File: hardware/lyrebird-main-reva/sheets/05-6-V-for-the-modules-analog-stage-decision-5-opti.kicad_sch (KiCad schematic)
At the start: 6 parts, among them U7 LMR33630 12V->-6V inverting

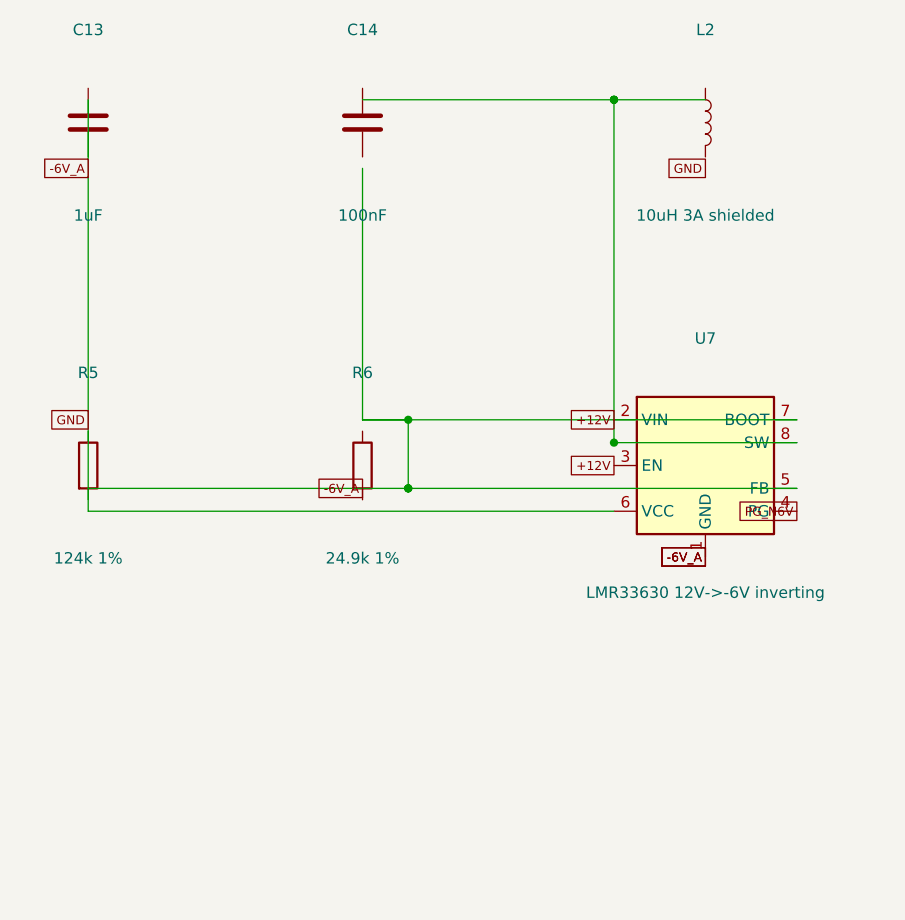
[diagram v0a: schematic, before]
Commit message: Connect two power-good nets that were connected to nothing
The schematic validator found a confirmed fault, and it is the kind that
reads as correct code. `Net("PG_5V")` appears twice in main_board.py --
once to attach the buck's power-good pin, once to attach its pull-up --
and SKiDL creates a NEW net on each call, uniquifying the second name.
The result was four single-node nets: both LMR33630 power-good pins
alone, and both 100 k resistors with one lead floating.

The inverter's half mattered more than the buck's. U7's GND pin *is*
-6V_A, so 100 k to system ground is a pull-up relative to the device and
the only way that flag can be read at all. It was reading nothing.

Both now use one Net object and reuse it, which is what every other net
in both generators already did -- the defect was exactly two instances of
one idiom, not a pattern. I checked: MCLK is also written as
Net("MCLK") twice, but once per file on different boards, so it is
whole in each netlist.

The more useful outcome is a check. A net with one node connects
nothing, and nothing in the generation path said so -- KiCad ERC would
have, on import, and nothing runs ERC. check_freshness.py now reports
single-node nets on both boards, with the module's four reserved element
lines exempted because interface.md requires the main board to drive
them and they are correctly bare on the module side. Tamper-tested by
reintroducing the idiom: it names PG_5V and PG_5V1 and fails.

Co-Authored-By: Claude Opus 5 <noreply@anthropic.com>
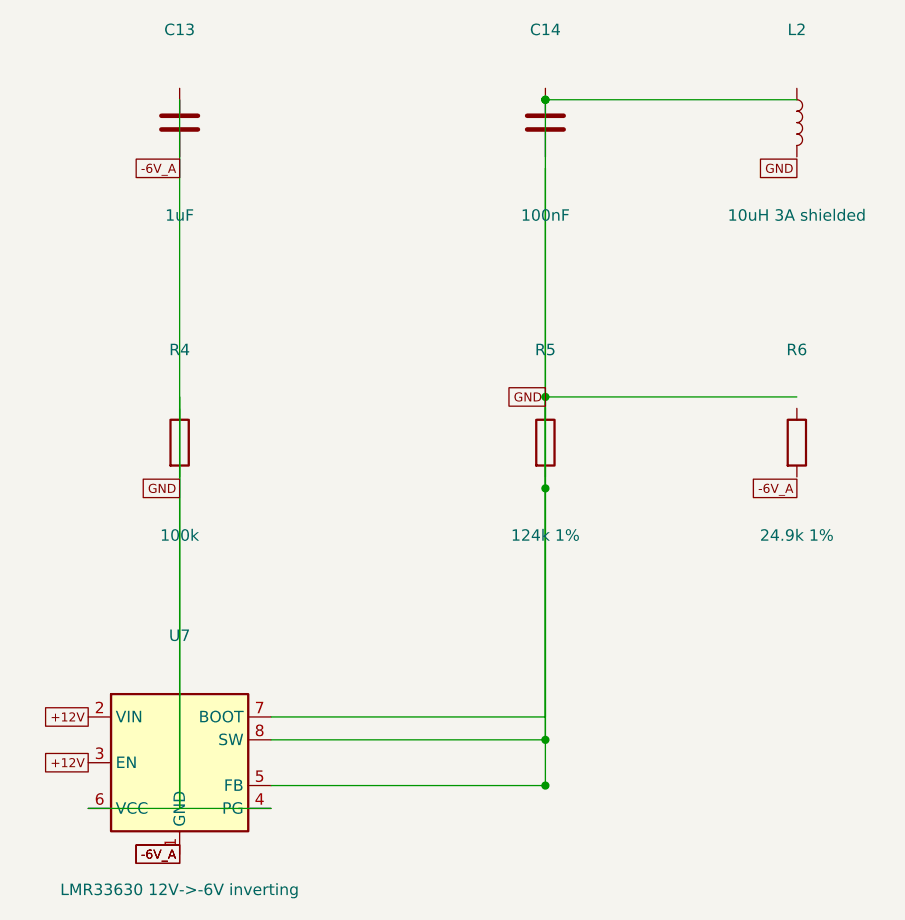
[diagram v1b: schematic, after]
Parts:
- added U7: LMR33630 12V->-6V inverting, symbol Regulator_Switching:LMR33630ADDA
- R4: renamed from R5; value 124k 1% -> 100k
- R5: renamed from R6; value 24.9k 1% -> 124k 1%
- R6: renamed from U7; value LMR33630 12V->-6V inverting -> 24.9k 1%; symbol Regulator_Switching:LMR33630ADDA -> Device:R
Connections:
- net +12V: now also U7.2 (VIN), U7.3 (EN); no longer R6.1 (GND), R6.2 (VIN), R6.3 (EN), R6.5 (FB), R6.6 (VCC), R6.7 (BOOT), R6.8 (SW), R6.9 (GND)
- removed net PG_N6V: R6.4 (PG)
- new net -6V_A: U7.1 (GND), U7.4 (PG), U7.5 (FB), U7.6 (VCC), U7.7 (BOOT), U7.8 (SW), U7.9 (GND)
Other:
- moved on the sheet: C13, C14, L2, R4, R5
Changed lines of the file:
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@@
 	(version 20231120)
 	(generator "lyrebird")
-	(paper "User" 164 115)
+	(paper "User" 164 148)
 	(title_block (title "6 V for the module's analog stage (decision 5, option B)"))
-	(symbol (lib_id "Device:C") (at 35.56 35.56 0) (unit 1)
+	(symbol (lib_id "Device:C") (at 45.72 35.56 0) (unit 1)
 		(exclude_from_sim no) (in_bom yes) (on_board yes) (dnp no)
-		(property "Reference" "C13" (at 35.56 25.250000000000004 0)
+		(property "Reference" "C13" (at 45.72 25.250000000000004 0)
 			(effects (font (size 1.27 1.27))))
-		(property "Value" "1uF" (at 35.56 45.870000000000005 0)
+		(property "Value" "1uF" (at 45.72 45.870000000000005 0)
 			(effects (font (size 1.27 1.27))))
 		(instances (project "" (path "/" (reference "C13") (unit 1))))
 	)
-	(symbol (lib_id "Device:C") (at 66.04 35.56 0) (unit 1)
+	(symbol (lib_id "Device:C") (at 86.36 35.56 0) (unit 1)
 		(exclude_from_sim no) (in_bom yes) (on_board yes) (dnp no)
-		(property "Reference" "C14" (at 66.04 25.250000000000004 0)
+		(property "Reference" "C14" (at 86.36 25.250000000000004 0)
 			(effects (font (size 1.27 1.27))))
-		(property "Value" "100nF" (at 66.04 45.870000000000005 0)
+		(property "Value" "100nF" (at 86.36 45.870000000000005 0)
 			(effects (font (size 1.27 1.27))))
 		(instances (project "" (path "/" (reference "C14") (unit 1))))
 	)
-	(symbol (lib_id "Device:L") (at 104.14 35.56 0) (unit 1)
+	(symbol (lib_id "Device:L") (at 114.3 35.56 0) (unit 1)
 		(exclude_from_sim no) (in_bom yes) (on_board yes) (dnp no)
-		(property "Reference" "L2" (at 104.14 25.250000000000004 0)
+		(property "Reference" "L2" (at 114.3 25.250000000000004 0)
 			(effects (font (size 1.27 1.27))))
-		(property "Value" "10uH 3A shielded" (at 104.14 45.870000000000005 0)
+		(property "Value" "10uH 3A shielded" (at 114.3 45.870000000000005 0)
 			(effects (font (size 1.27 1.27))))
 		(instances (project "" (path "/" (reference "L2") (unit 1))))
 	)
-	(symbol (lib_id "Device:R") (at 35.56 73.66 0) (unit 1)
+	(symbol (lib_id "Device:R") (at 45.72 71.12 0) (unit 1)
 		(exclude_from_sim no) (in_bom yes) (on_board yes) (dnp no)
-		(property "Reference" "R5" (at 35.56 63.349999999999994 0)
+		(property "Reference" "R4" (at 45.72 60.81 0)
 			(effects (font (size 1.27 1.27))))
-		(property "Value" "124k 1%" (at 35.56 83.97 0)
+		(property "Value" "100k" (at 45.72 81.43 0)
+			(effects (font (size 1.27 1.27))))
+		(instances (project "" (path "/" (reference "R4") (unit 1))))
+	)
+	(symbol (lib_id "Device:R") (at 86.36 71.12 0) (unit 1)
+		(exclude_from_sim no) (in_bom yes) (on_board yes) (dnp no)
+		(property "Reference" "R5" (at 86.36 60.81 0)
+			(effects (font (size 1.27 1.27))))
+		(property "Value" "124k 1%" (at 86.36 81.43 0)
 			(effects (font (size 1.27 1.27))))
 		(instances (project "" (path "/" (reference "R5") (unit 1))))
 	)
-	(symbol (lib_id "Device:R") (at 66.04 73.66 0) (unit 1)
+	(symbol (lib_id "Device:R") (at 114.3 71.12 0) (unit 1)
 		(exclude_from_sim no) (in_bom yes) (on_board yes) (dnp no)
-		(property "Reference" "R6" (at 66.04 63.349999999999994 0)
+		(property "Reference" "R6" (at 114.3 60.81 0)
 			(effects (font (size 1.27 1.27))))
-		(property "Value" "24.9k 1%" (at 66.04 83.97 0)
+		(property "Value" "24.9k 1%" (at 114.3 81.43 0)
 			(effects (font (size 1.27 1.27))))
 		(instances (project "" (path "/" (reference "R6") (unit 1))))
 	)
-	(symbol (lib_id "Regulator_Switching:LMR33630ADDA") (at 104.14 73.66 0) (unit 1)
+	(symbol (lib_id "Regulator_Switching:LMR33630ADDA") (at 45.72 106.68 0) (unit 1)
 		(exclude_from_sim no) (in_bom yes) (on_board yes) (dnp no)
-		(property "Reference" "U7" (at 104.14 59.53999999999999 0)
+		(property "Reference" "U7" (at 45.72 92.56 0)
 			(effects (font (size 1.27 1.27))))
-		(property "Value" "LMR33630 12V->-6V inverting" (at 104.14 87.78 0)
+		(property "Value" "LMR33630 12V->-6V inverting" (at 45.72 120.80000000000001 0)
 			(effects (font (size 1.27 1.27))))
 		(instances (project "" (path "/" (reference "U7") (unit 1))))
 	)
-	(wire (pts (xy 71.12 68.58) (xy 71.12 76.2))
+	(wire (pts (xy 86.36 66.04) (xy 86.36 109.22))
 		(stroke (width 0) (type default)))
-	(wire (pts (xy 35.56 76.2) (xy 71.12 76.2))
+	(junction (at 86.36 76.2) (diameter 0)
+		(color 0 0 0 0))
+	(wire (pts (xy 114.3 66.04) (xy 86.36 66.04))
 		(stroke (width 0) (type default)))
-	(junction (at 71.12 76.2) (diameter 0)
+	(junction (at 86.36 66.04) (diameter 0)
 		(color 0 0 0 0))
-	(wire (pts (xy 66.04 68.58) (xy 71.12 68.58))
+	(wire (pts (xy 55.88 109.22) (xy 86.36 109.22))
 		(stroke (width 0) (type default)))
-	(junction (at 71.12 68.58) (diameter 0)
+	(junction (at 86.36 109.22) (diameter 0)
 		(color 0 0 0 0))
-	(wire (pts (xy 114.3 76.2) (xy 71.12 76.2))
+	(wire (pts (xy 45.72 33.02) (xy 45.72 111.76))
 		(stroke (width 0) (type default)))
-	(junction (at 71.12 76.2) (diameter 0)
+	(wire (pts (xy 45.72 111.76) (xy 35.56 111.76))
+		(stroke (width 0) (type default)))
+	(wire (pts (xy 86.36 40.64) (xy 86.36 101.6))
+		(stroke (width 0) (type default)))
+	(wire (pts (xy 86.36 101.6) (xy 55.88 101.6))
+		(stroke (width 0) (type default)))
+	(wire (pts (xy 45.72 66.04) (xy 45.72 111.76))
+		(stroke (width 0) (type default)))
+	(wire (pts (xy 45.72 111.76) (xy 55.88 111.76))
+		(stroke (width 0) (type default)))
+	(wire (pts (xy 86.36 33.02) (xy 86.36 104.14))
+		(stroke (width 0) (type default)))
+	(junction (at 86.36 33.02) (diameter 0)
 		(color 0 0 0 0))
-	(wire (pts (xy 35.56 33.02) (xy 35.56 78.74))
+	(wire (pts (xy 114.3 33.02) (xy 86.36 33.02))
 		(stroke (width 0) (type default)))
-	(wire (pts (xy 35.56 78.74) (xy 93.98 78.74))
+	(junction (at 86.36 33.02) (diameter 0)
+		(color 0 0 0 0))
+	(wire (pts (xy 55.88 104.14) (xy 86.36 104.14))
 		(stroke (width 0) (type default)))
-	(wire (pts (xy 66.04 40.64) (xy 66.04 68.58))
-		(stroke (width 0) (type default)))
-	(wire (pts (xy 66.04 68.58) (xy 114.3 68.58))
-		(stroke (width 0) (type default)))
-	(wire (pts (xy 93.98 33.02) (xy 93.98 71.12))
-		(stroke (width 0) (type default)))
-	(wire (pts (xy 66.04 33.02) (xy 93.98 33.02))
-		(stroke (width 0) (type default)))
-	(junction (at 93.98 33.02) (diameter 0)
+	(junction (at 86.36 104.14) (diameter 0)
 		(color 0 0 0 0))
-	(wire (pts (xy 104.14 33.02) (xy 93.98 33.02))
-		(stroke (width 0) (type default)))
-	(junction (at 93.98 33.02) (diameter 0)
-		(color 0 0 0 0))
-	(wire (pts (xy 114.3 71.12) (xy 93.98 71.12))
-		(stroke (width 0) (type default)))
-	(junction (at 93.98 71.12) (diameter 0)
-		(color 0 0 0 0))
-	(global_label "+12V" (shape passive) (at 93.98 68.58 0)
+	(global_label "+12V" (shape passive) (at 35.56 101.6 0)
 		(effects (font (size 1.0 1.0)) (justify right))
 )
-	(global_label "+12V" (shape passive) (at 93.98 73.66 0)
+	(global_label "+12V" (shape passive) (at 35.56 106.68 0)
 		(effects (font (size 1.0 1.0)) (justify right))
 )
-	(global_label "-6V_A" (shape passive) (at 35.56 40.64 0)
+	(global_label "-6V_A" (shape passive) (at 45.72 40.64 0)
 		(effects (font (size 1.0 1.0)) (justify right))
 )
-	(global_label "-6V_A" (shape passive) (at 66.04 76.2 0)
+	(global_label "-6V_A" (shape passive) (at 114.3 76.2 0)
 		(effects (font (size 1.0 1.0)) (justify right))
 )
-	(global_label "-6V_A" (shape passive) (at 104.14 83.82000000000001 0)
+	(global_label "-6V_A" (shape passive) (at 45.72 116.84 0)
 		(effects (font (size 1.0 1.0)) (justify right))
 )
-	(global_label "-6V_A" (shape passive) (at 104.14 83.82000000000001 0)
+	(global_label "-6V_A" (shape passive) (at 45.72 116.84 0)
 		(effects (font (size 1.0 1.0)) (justify right))
 )
-	(global_label "GND" (shape passive) (at 104.14 40.64 0)
+	(global_label "GND" (shape passive) (at 114.3 40.64 0)
 		(effects (font (size 1.0 1.0)) (justify right))
 )
-	(global_label "GND" (shape passive) (at 35.56 68.58 0)
+	(global_label "GND" (shape passive) (at 45.72 76.2 0)
 		(effects (font (size 1.0 1.0)) (justify right))
 )
-	(global_label "PG_N6V" (shape passive) (at 114.3 78.74 0)
+	(global_label "GND" (shape passive) (at 86.36 66.04 0)
 		(effects (font (size 1.0 1.0)) (justify right))
 )
